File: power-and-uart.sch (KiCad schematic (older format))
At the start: 41 parts, among them J1 USB_miniB, J2 USB_C_Receptacle, U1 USB3740B-AI9, U2 UTC2000, U3 FT232RL, U4 74LVC1G00, U5 SC185

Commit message: replaced resistor symbols with originals from trigbox.lib
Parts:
- R1, R14, R15, R16, R17, R18, R2: symbol power-test-module-rescue:R100k-trigbox -> trigbox:R100k
- R10, R5, R6, R8, R9: symbol power-test-module-rescue:R10k-trigbox -> trigbox:R10k
- R7: symbol power-test-module-rescue:R4k7-trigbox -> trigbox:R4k7
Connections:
- net labels removed: VIN
- wire segments 138 -> 137
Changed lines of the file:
@@
 	4100 7500 4300 7500
 $Comp
-L power-test-module-rescue:R10k-trigbox R8
+L trigbox:R10k R8
 U 1 1 5C383AE5
 P 4300 7400
@@
 	4300 7500 4600 7500
 $Comp
-L power-test-module-rescue:R4k7-trigbox R7
+L trigbox:R4k7 R7
 U 1 1 5C383AEE
 P 4300 6700
@@
 	3900 5950 3550 5950
 $Comp
-L power-test-module-rescue:R100k-trigbox R1
+L trigbox:R100k R1
 U 1 1 5C383B4A
 P 3300 6700
@@
 $EndComp
 $Comp
-L power-test-module-rescue:R100k-trigbox R2
+L trigbox:R100k R2
 U 1 1 5C383B51
 P 3300 6900
@@
 Wire Wire Line
 	3000 5950 3050 5950
-$Comp
-L power-test-module-rescue:VIN-trigbox #PWR?
-U 1 1 5C3CF01A
-P 7900 1000
-AR Path="/5C3C60AE/5C3CF01A" Ref="#PWR?"  Part="1"
-AR Path="/5C3CF01A" Ref="#PWR?"  Part="1"
-AR Path="/5C4CE703/5C3CF01A" Ref="#PWR?"  Part="1"
-F 0 "#PWR?" H 7900 850 50  0001 C CNN
-F 1 "VIN" H 7915 1173 50  0000 C CNN
-F 2 "" H 7900 1000 50  0001 C CNN
-F 3 "" H 7900 1000 50  0001 C CNN
-	1    7900 1000
-	1    0    0    -1
-$EndComp
-Wire Wire Line
-	7900 1000 8100 1000
 $Comp
 L power:PWR_FLAG #FLG?
@@
 Wire Wire Line
 	6800 2050 6800 2450
-Wire Wire Line
-	7200 1000 7900 1000
 Connection ~ 7200 1000
-Connection ~ 7900 1000
 $Comp
 L power:+5V #PWR?
@@
 $EndComp
 $Comp
-L power-test-module-rescue:R10k-trigbox R?
+L trigbox:R10k R?
 U 1 1 5C3CF0FC
 P 4200 3300
@@
 $EndComp
 $Comp
-L power-test-module-rescue:R10k-trigbox R?
+L trigbox:R10k R?
 U 1 1 5C3CF103
 P 4100 3300
@@
 $EndComp
 $Comp
-L power-test-module-rescue:R10k-trigbox R?
+L trigbox:R10k R?
 U 1 1 5C3CF124
 P 3450 3500
@@
 $EndComp
 $Comp
-L power-test-module-rescue:R10k-trigbox R?
+L trigbox:R10k R?
 U 1 1 5C3CF12B
 P 3550 3500
@@
 	4100 4600 4100 4750
 $Comp
-L power-test-module-rescue:R100k-trigbox R?
+L trigbox:R100k R?
 U 1 1 5C3CF184
 P 5550 3750
@@
 Alt: CDMC6D28NP-1RØMC
 $Comp
-L power-test-module-rescue:R100k-trigbox R?
+L trigbox:R100k R?
 U 1 1 5C3EC942
 P 5800 3750
@@
 	5350 4800 4000 4800
 $Comp
-L power-test-module-rescue:R100k-trigbox R?
+L trigbox:R100k R?
 U 1 1 5C417A62
 P 5000 4300
@@
 $EndComp
 $Comp
-L power-test-module-rescue:R100k-trigbox R?
+L trigbox:R100k R?
 U 1 1 5C417B66
 P 5350 4300
@@
 $EndComp
 $Comp
-L power-test-module-rescue:R100k-trigbox R?
+L trigbox:R100k R?
 U 1 1 5C417BFB
 P 6850 3400
@@
 	1    0    0    -1
 $EndComp
+Wire Wire Line
+	7200 1000 8100 1000
 $EndSCHEMATC

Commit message: replaced all rescued symbols by originals from trigbox.lib; removed rescue.lib
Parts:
- C3, C5, C7: symbol power-test-module-rescue:22uF_lo_ESR-trigbox -> trigbox:22uF_lo_ESR
- U5: symbol power-test-module-rescue:SC185-trigbox -> trigbox:SC185
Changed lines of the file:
@@
 	8100 1000 8300 1000
-$Comp
-L power-test-module-rescue:SC185-trigbox U?
-U 1 1 5C3CF031
-P 6250 2100
-AR Path="/5C3C60AE/5C3CF031" Ref="U?"  Part="1"
-AR Path="/5C3CF031" Ref="U5"  Part="1"
-AR Path="/5C4CE703/5C3CF031" Ref="U5"  Part="1"
-F 0 "U5" H 6250 3010 50  0000 C CNN
-F 1 "SC185" H 6250 2919 50  0000 C CNN
-F 2 "Package_DFN_QFN:QFN-16-1EP_3x3mm_P0.5mm_EP1.8x1.8mm" H 6150 2000 50  0001 C CNN
-F 3 "" H 6250 2100 50  0001 C CNN
-F 4 "SC185QULTRT (3.3V)" H 6250 2828 50  0000 C CNN "Part"
-F 5 "Semtech" H 6250 2737 50  0000 C CNN "Manufacturer"
-	1    6250 2100
-	1    0    0    -1
-$EndComp
 $Comp
 L Device:L_Core_Ferrite L?
@@
 $EndComp
 $Comp
-L power-test-module-rescue:22uF_lo_ESR-trigbox C?
+L trigbox:22uF_lo_ESR C?
 U 1 1 5C3CF043
 P 5050 2100
@@
 Wire Wire Line
 	5700 1950 5700 2050
-Connection ~ 5700 2050
 Wire Wire Line
 	5050 1950 5300 1950
@@
 	5700 2700 5600 2700
 Connection ~ 5600 2700
-Wire Wire Line
-	5700 2150 5700 2700
 $Comp
 L power:GND #PWR?
@@
 	1    0    0    -1
 $EndComp
-Connection ~ 6800 2450
-Wire Wire Line
-	6800 1950 6800 2050
-Connection ~ 6800 2050
 Wire Wire Line
 	6400 1550 6800 1550
 Wire Wire Line
-	6800 1550 6800 1950
-Connection ~ 6800 1950
-Wire Wire Line
-	6300 1550 6200 1550
-Wire Wire Line
-	6200 1550 6100 1550
-Connection ~ 6200 1550
-Wire Wire Line
 	6100 1550 6100 1000
 Wire Wire Line
 	6100 1000 6650 1000
-Connection ~ 6100 1550
-$Comp
-L power-test-module-rescue:22uF_lo_ESR-trigbox C?
+$Comp
+L trigbox:22uF_lo_ESR C?
 U 1 1 5C3CF098
 P 6950 1150
@@
 $EndComp
 $Comp
-L power-test-module-rescue:22uF_lo_ESR-trigbox C?
+L trigbox:22uF_lo_ESR C?
 U 1 1 5C3CF0A1
 P 7200 1150
@@
 Wire Wire Line
 	7100 1000 6950 1000
-Wire Wire Line
-	6800 2050 6800 2450
 Connection ~ 7200 1000
 $Comp
@@
 Wire Wire Line
 	7200 1000 8100 1000
+Wire Wire Line
+	5700 2150 5700 2700
+Connection ~ 5700 2050
+Connection ~ 6800 2450
+Connection ~ 6100 1550
+Wire Wire Line
+	6200 1550 6100 1550
+Wire Wire Line
+	6300 1550 6200 1550
+Connection ~ 6200 1550
+Wire Wire Line
+	6800 1550 6800 1950
+Connection ~ 6800 1950
+Wire Wire Line
+	6800 2050 6800 2450
+Wire Wire Line
+	6800 1950 6800 2050
+Connection ~ 6800 2050
+$Comp
+L trigbox:SC185 U?
+U 1 1 5C3CF031
+P 6250 2100
+AR Path="/5C3C60AE/5C3CF031" Ref="U?"  Part="1"
+AR Path="/5C3CF031" Ref="U5"  Part="1"
+AR Path="/5C4CE703/5C3CF031" Ref="U5"  Part="1"
+F 0 "U5" H 6250 3010 50  0000 C CNN
+F 1 "SC185" H 6250 2919 50  0000 C CNN
+F 2 "Package_DFN_QFN:QFN-16-1EP_3x3mm_P0.5mm_EP1.8x1.8mm" H 6150 2000 50  0001 C CNN
+F 3 "" H 6250 2100 50  0001 C CNN
+F 4 "SC185QULTRT (3.3V)" H 6250 2828 50  0000 C CNN "Part"
+F 5 "Semtech" H 6250 2737 50  0000 C CNN "Manufacturer"
+	1    6250 2100
+	1    0    0    -1
+$EndComp
 $EndSCHEMATC

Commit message: re-annotated with base number 1000
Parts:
- renumbered C1 to C1001, C8 to C1002, C2 to C1003, C3 to C1004, C4 to C1005, C5 to C1006, C6 to C1007, C7 to C1008, D2 to D1001, D3 to D1002, D1 to D1003, FL1 to FL1001, FL2 to FL1002, J1 to J1002, J2 to J1003, JP1 to JP1001, JP2 to JP1002, L1 to L1001, R3 to R1001, R1 to R1002, R2 to R1003, R4 to R1004, R5 to R1005, R6 to R1006, R9 to R1007, R10 to R1008, R11 to R1009, R7 to R1010, R8 to R1011, R12 to R1012, R15 to R1013, R16 to R1014, R13 to R1015, R14 to R1016, R17 to R1017, R18 to R1018, U1 to U1001, U2 to U1002, U3 to U1003, U4 to U1004, U5 to U1005

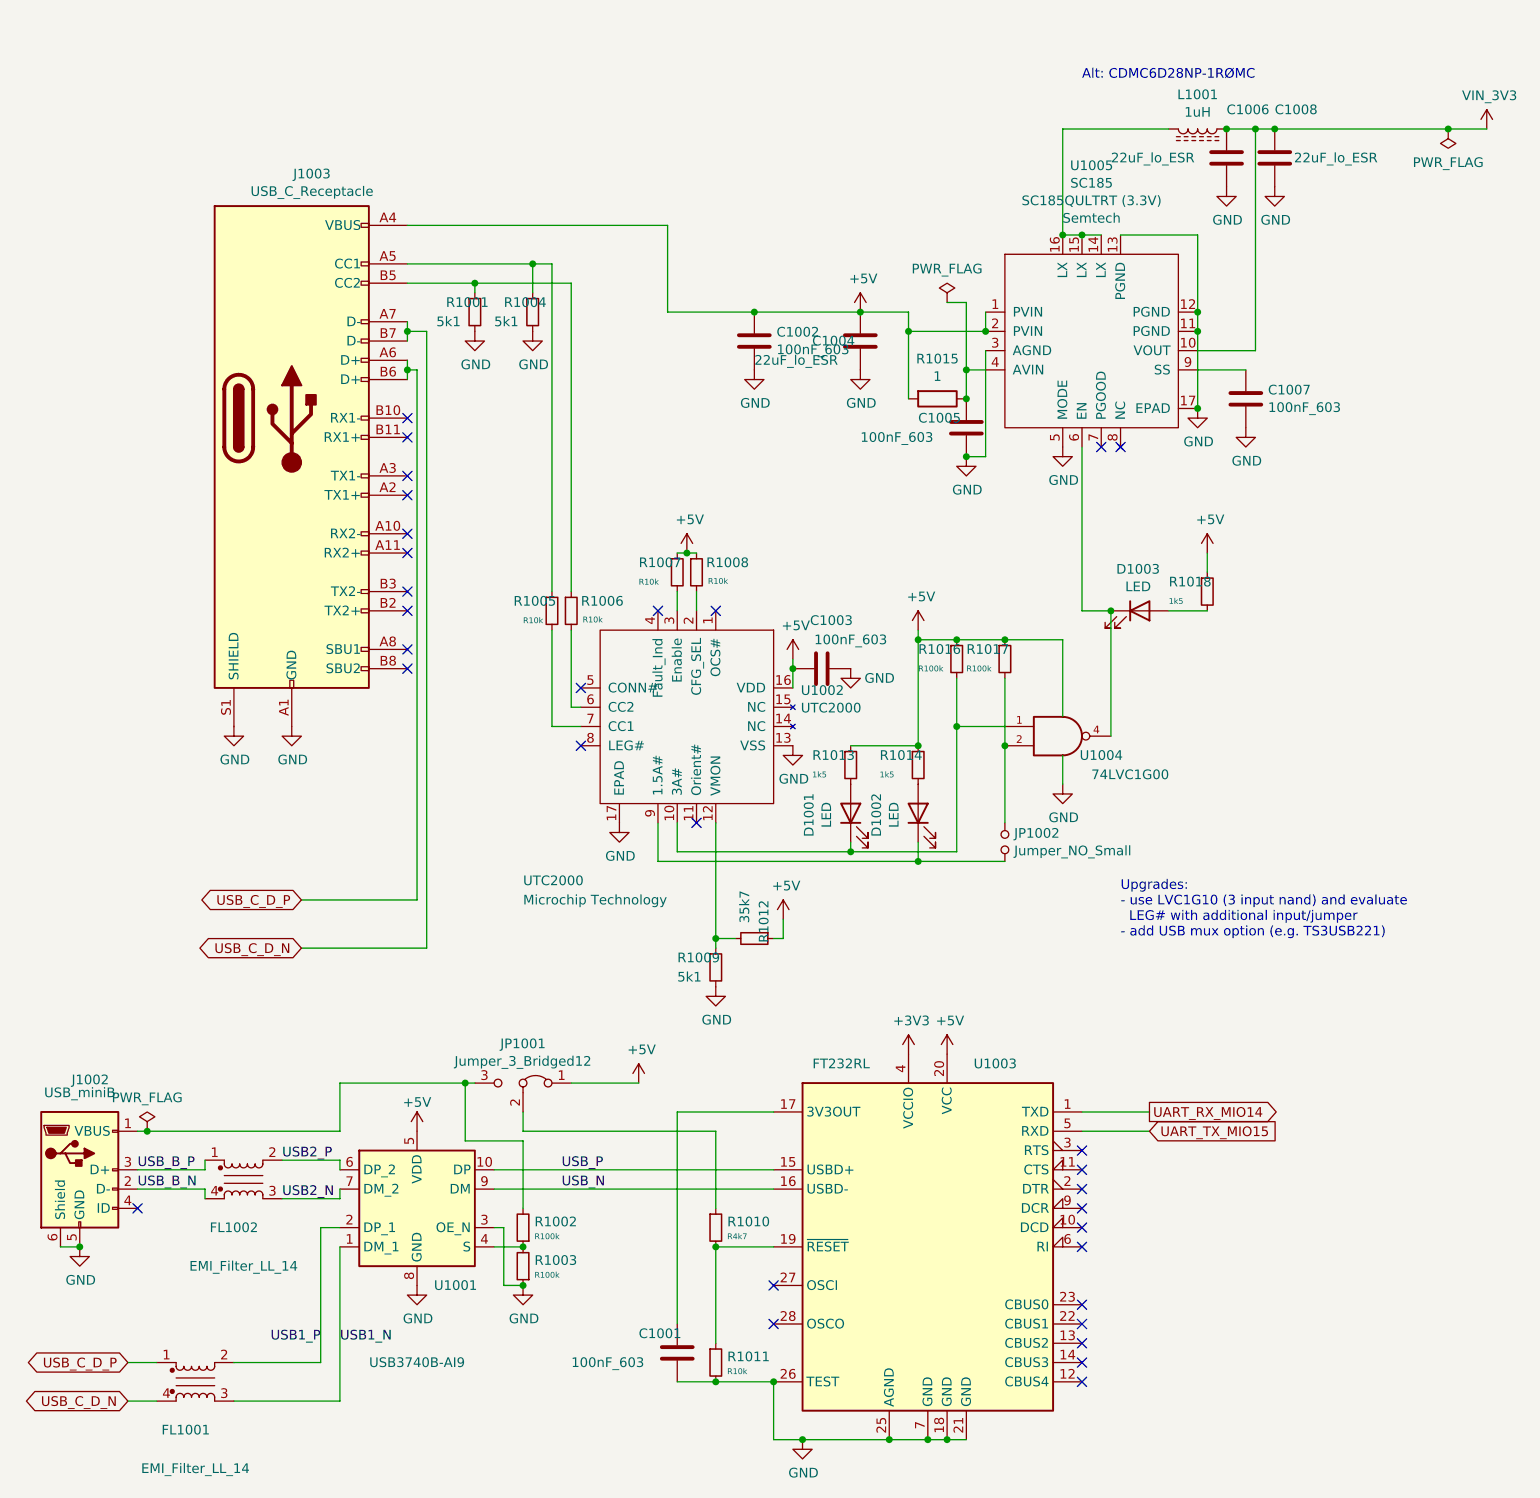
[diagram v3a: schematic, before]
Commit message: use hierarchical labels from power-and-uart sheet
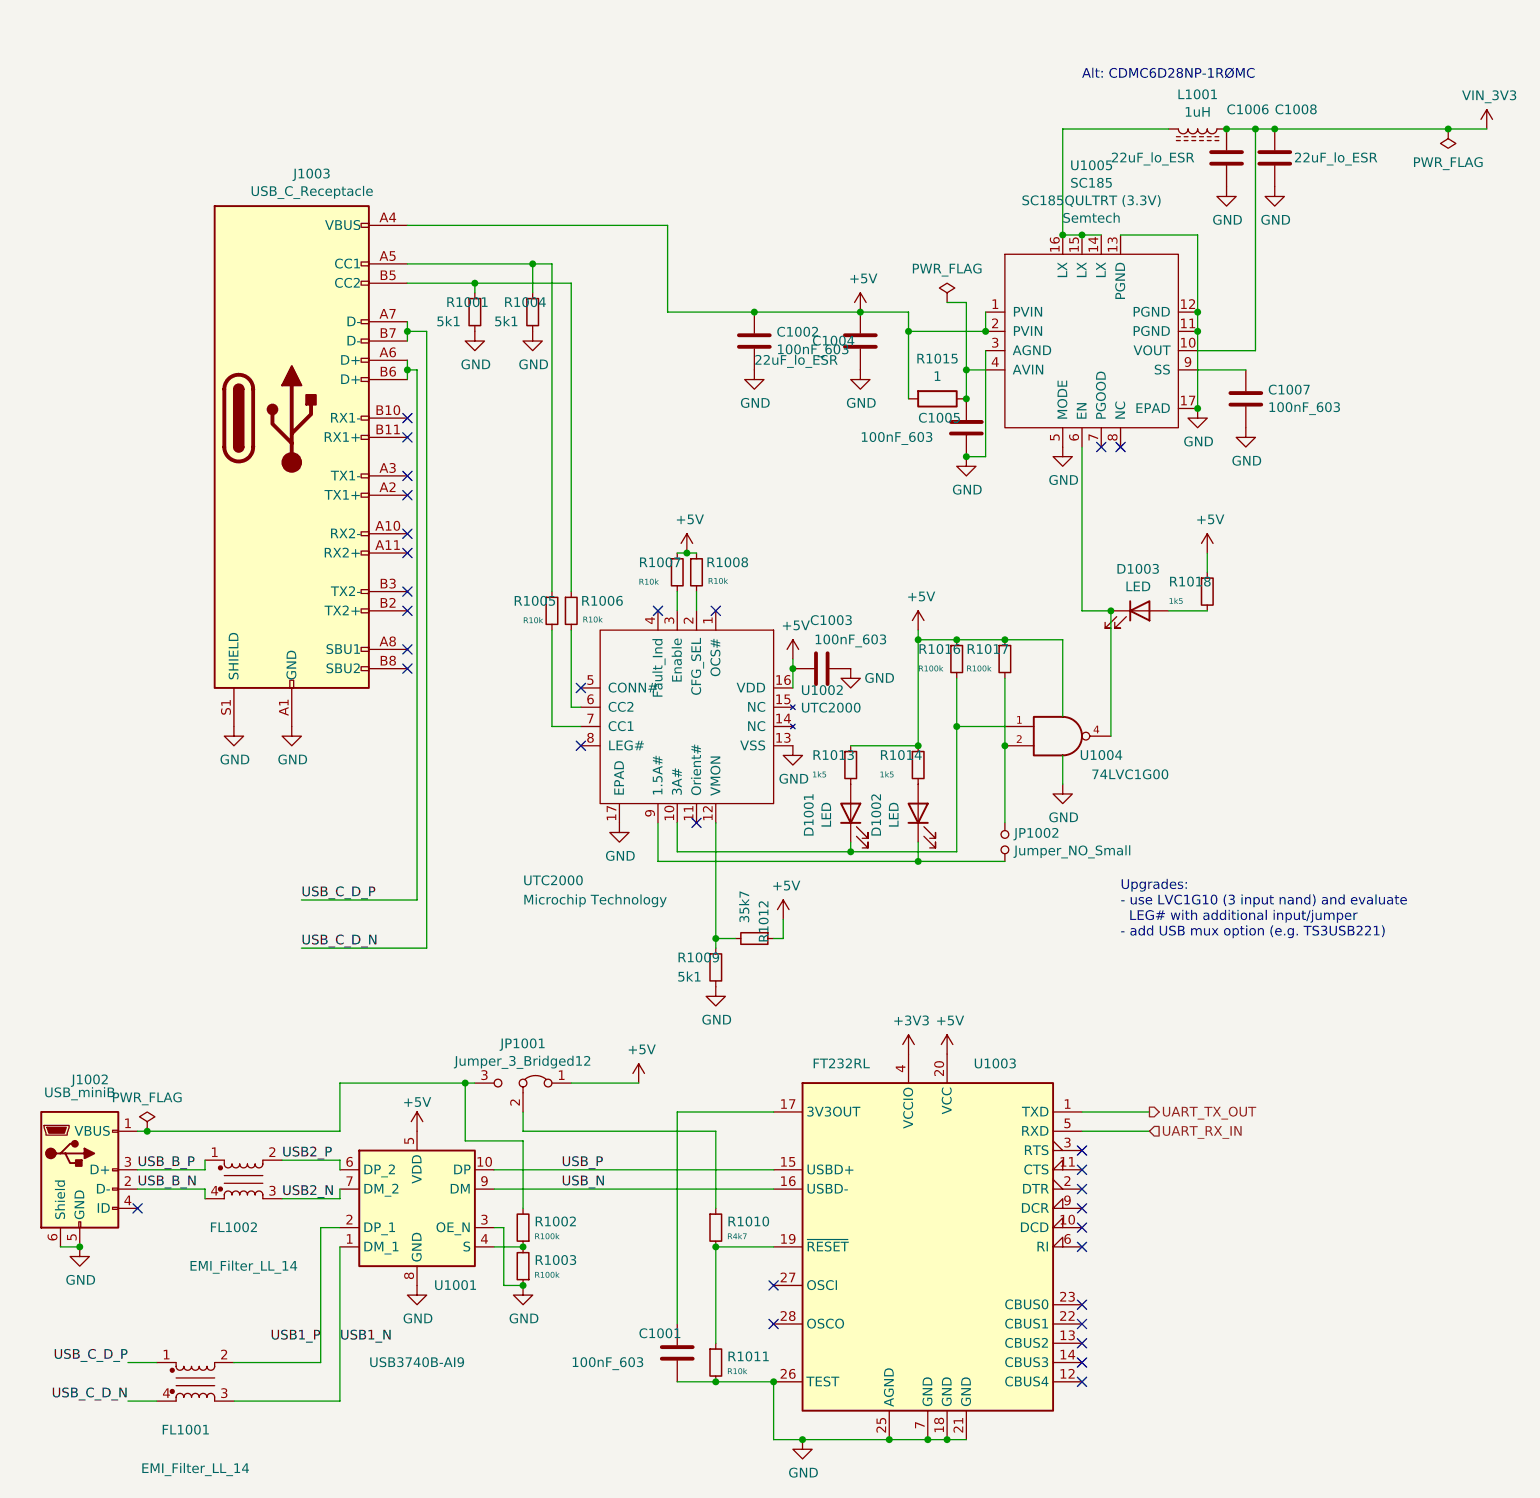
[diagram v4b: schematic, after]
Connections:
- net UART_RX_MIO14 renamed UART_TX_OUT
- net UART_TX_MIO15 renamed UART_RX_IN
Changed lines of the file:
@@
 NoConn ~ 6200 6700
 NoConn ~ 6200 6800
-Text GLabel 1250 7400 0    50   BiDi ~ 0
-USB_C_D_P
-Text GLabel 1250 7600 0    50   BiDi ~ 0
-USB_C_D_N
 $Comp
 L Interface_USB:USB3740B-AI9 U1001
@@
 Wire Wire Line
 	2700 2200 2700 2250
-Text GLabel 2150 5000 0    50   BiDi ~ 0
-USB_C_D_P
-Text GLabel 2150 5250 0    50   BiDi ~ 0
-USB_C_D_N
 Wire Wire Line
 	2700 2250 2750 2250
@@
 	1    0    0    -1
 $EndComp
-Text GLabel 6550 6100 2    50   Output ~ 0
-UART_RX_MIO14
-Text GLabel 6550 6200 2    50   Input ~ 0
-UART_TX_MIO15
 Wire Wire Line
 	6200 6100 6550 6100
@@
 	1    0    0    -1
 $EndComp
+Text Label 2150 5000 0    50   ~ 0
+USB_C_D_P
+Text Label 1250 7400 2    50   ~ 0
+USB_C_D_P
+Text Label 1250 7600 2    50   ~ 0
+USB_C_D_N
+Text Label 2150 5250 0    50   ~ 0
+USB_C_D_N
+Text HLabel 6550 6100 2    50   Output ~ 0
+UART_TX_OUT
+Text HLabel 6550 6200 2    50   Input ~ 0
+UART_RX_IN
 $EndSCHEMATC

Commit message: use QFN-16 footprint from proj-library
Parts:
- U1002, U1005: footprint Package_DFN_QFN:QFN-16-1EP_3x3mm_P0.5mm_EP1.8x1.8mm -> proj_footprints:QFN-16-1EP_3x3mm_P0.5mm_EP1.8x1.8mm
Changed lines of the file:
@@
 F 0 "U1002" V 4013 4641 50  0000 L CNN
 F 1 "UTC2000" V 4104 4641 50  0000 L CNN
-F 2 "Package_DFN_QFN:QFN-16-1EP_3x3mm_P0.5mm_EP1.8x1.8mm" H 4050 3950 50  0001 C CNN
+F 2 "proj_footprints:QFN-16-1EP_3x3mm_P0.5mm_EP1.8x1.8mm" H 4050 3950 50  0001 C CNN
 F 3 "" H 4150 4050 50  0001 C CNN
 F 4 "UTC2000" V 5000 3200 50  0000 L CNN "Part"
@@
 F 0 "U1005" H 6250 3010 50  0000 C CNN
 F 1 "SC185" H 6250 2919 50  0000 C CNN
-F 2 "Package_DFN_QFN:QFN-16-1EP_3x3mm_P0.5mm_EP1.8x1.8mm" H 6150 2000 50  0001 C CNN
+F 2 "proj_footprints:QFN-16-1EP_3x3mm_P0.5mm_EP1.8x1.8mm" H 6150 2000 50  0001 C CNN
 F 3 "" H 6250 2100 50  0001 C CNN
 F 4 "SC185QULTRT (3.3V)" H 6250 2828 50  0000 C CNN "Part"

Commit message: swapped USBC connector; jlcpcb hole distance.
- use usbc-usb2.0 variant with more power pins
- enforce .5mm hole spacing (jlcpcb)
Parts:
- removed J1003: USB_C_Receptacle, Connector_USB:USB_C_Receptacle_Amphenol_12401610E4-2A_CircularHoles, symbol Connector:USB_C_Receptacle
- added J1003: USB_C_Receptacle_USB2.0, proj_footprints:USB_C_Receptacle_GCT_USB4085_smaller_holes, symbol Connector:USB_C_Receptacle_USB2.0
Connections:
- net +5V: now also J1003.A4 (VBUS), J1003.A9 (VBUS), J1003.B4 (VBUS), J1003.B9 (VBUS)
- net GND: now also J1003.A1 (GND), J1003.A12 (GND), J1003.B1 (GND), J1003.B12 (GND), J1003.S1 (SHIELD)
- net USB1_N: now also FL1001.2; no longer FL1001.3
- net USB1_P: now also FL1001.3; no longer FL1001.2
- net USB_C_D_N: now also FL1001.1, J1003.A7 (D-), J1003.B7 (D-); no longer FL1001.4
- net USB_C_D_P: now also FL1001.4, J1003.A6 (D+), J1003.B6 (D+); no longer FL1001.1
- net at R1004.1, R1005.1: now also J1003.A5 (CC1)
- net at R1001.1, R1006.1: now also J1003.B5 (CC2)
- no-connect marks 31 -> 23
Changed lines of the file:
@@
 F 3 "https://www.digikey.com/catalog/en/partgroup/we-cnsw-we-cnsw-hf/22783?mpart=744231371&vendor=732" H 1600 7687 50  0001 C CNN
 	1    1600 7500
-	1    0    0    -1
+	1    0    0    1
 $EndComp
 Wire Wire Line
@@
 	1    0    0    -1
 $EndComp
-$Comp
-L Connector:USB_C_Receptacle J?
-U 1 1 5C3CF0CC
-P 2100 2500
-AR Path="/5C3CF0CC" Ref="J?"  Part="1"
-AR Path="/5CEAC2F1/5C3CF0CC" Ref="J?"  Part="1"
-AR Path="/5C3C60AE/5C3CF0CC" Ref="J?"  Part="1"
-AR Path="/5C4CE703/5C3CF0CC" Ref="J1003"  Part="1"
-F 0 "J1003" H 2205 3767 50  0000 C CNN
-F 1 "USB_C_Receptacle" H 2205 3676 50  0000 C CNN
-F 2 "Connector_USB:USB_C_Receptacle_Amphenol_12401610E4-2A_CircularHoles" H 2250 2500 50  0001 C CNN
-F 3 "https://www.usb.org/sites/default/files/documents/usb_type-c.zip" H 2250 2500 50  0001 C CNN
-	1    2100 2500
-	1    0    0    -1
-$EndComp
 Wire Wire Line
 	2700 1500 4050 1500
@@
 L power:GND #PWR?
 U 1 1 5C3CF0D6
-P 2100 4100
+P 2100 3000
 AR Path="/5C3C60AE/5C3CF0D6" Ref="#PWR?"  Part="1"
 AR Path="/5C3CF0D6" Ref="#PWR?"  Part="1"
 AR Path="/5C4CE703/5C3CF0D6" Ref="#PWR?"  Part="1"
-F 0 "#PWR?" H 2100 3850 50  0001 C CNN
-F 1 "GND" H 2105 3927 50  0000 C CNN
-F 2 "" H 2100 4100 50  0001 C CNN
-F 3 "" H 2100 4100 50  0001 C CNN
-	1    2100 4100
+F 0 "#PWR?" H 2100 2750 50  0001 C CNN
+F 1 "GND" H 2105 2827 50  0000 C CNN
+F 2 "" H 2100 3000 50  0001 C CNN
+F 3 "" H 2100 3000 50  0001 C CNN
+	1    2100 3000
 	1    0    0    -1
 $EndComp
@@
 L power:GND #PWR?
 U 1 1 5C3CF0DC
-P 1800 4100
+P 1800 3000
 AR Path="/5C3C60AE/5C3CF0DC" Ref="#PWR?"  Part="1"
 AR Path="/5C3CF0DC" Ref="#PWR?"  Part="1"
 AR Path="/5C4CE703/5C3CF0DC" Ref="#PWR?"  Part="1"
-F 0 "#PWR?" H 1800 3850 50  0001 C CNN
-F 1 "GND" H 1805 3927 50  0000 C CNN
-F 2 "" H 1800 4100 50  0001 C CNN
-F 3 "" H 1800 4100 50  0001 C CNN
-	1    1800 4100
-	1    0    0    -1
-$EndComp
-NoConn ~ 2700 2500
+F 0 "#PWR?" H 1800 2750 50  0001 C CNN
+F 1 "GND" H 1805 2827 50  0000 C CNN
+F 2 "" H 1800 3000 50  0001 C CNN
+F 3 "" H 1800 3000 50  0001 C CNN
+	1    1800 3000
+	1    0    0    -1
+$EndComp
 NoConn ~ 2700 2600
-NoConn ~ 2700 2800
-NoConn ~ 2700 2900
-NoConn ~ 2700 3100
-NoConn ~ 2700 3200
-NoConn ~ 2700 3400
-NoConn ~ 2700 3500
-NoConn ~ 2700 3700
-NoConn ~ 2700 3800
 Wire Wire Line
 	2700 2000 2700 2050
@@
 Text HLabel 6550 6200 2    50   Input ~ 0
 UART_RX_IN
+$Comp
+L Connector:USB_C_Receptacle_USB2.0 J1003
+U 1 1 60DACEAD
+P 2100 2100
+F 0 "J1003" H 2207 2967 50  0000 C CNN
+F 1 "USB_C_Receptacle_USB2.0" H 2207 2876 50  0000 C CNN
+F 2 "proj_footprints:USB_C_Receptacle_GCT_USB4085_smaller_holes" H 2250 2100 50  0001 C CNN
+F 3 "https://www.usb.org/sites/default/files/documents/usb_type-c.zip" H 2250 2100 50  0001 C CNN
+	1    2100 2100
+	1    0    0    -1
+$EndComp
+NoConn ~ 2700 2700
 $EndSCHEMATC
